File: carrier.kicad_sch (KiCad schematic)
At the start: 54 parts, among them J1 Conn_02x06_Odd_Even, J10 Conn_01x02, J11 Conn_01x02, J12 AudioJack3_SwitchTR, J13 Conn_02x06_Odd_Even, J2 Conn_01x26, J3 Conn_01x26, J4 TYPE-C-31-M-12, J5 Conn_01x02, J6 Conn_01x02, J7 Conn_01x02, J8 Conn_01x02, J9 Conn_01x02, U1 CARAVEL, U2 W25Q128JVS, U3 LP5907MFX-3.3, U4 LP5907MFX-1.8, U5 LP5907MFX-1.8, U6 LP5907MFX-3.3, U7 TPD2E001DRSR, U8 OPA340NA, U9 OPA340NA, X1 SG-5032CAN

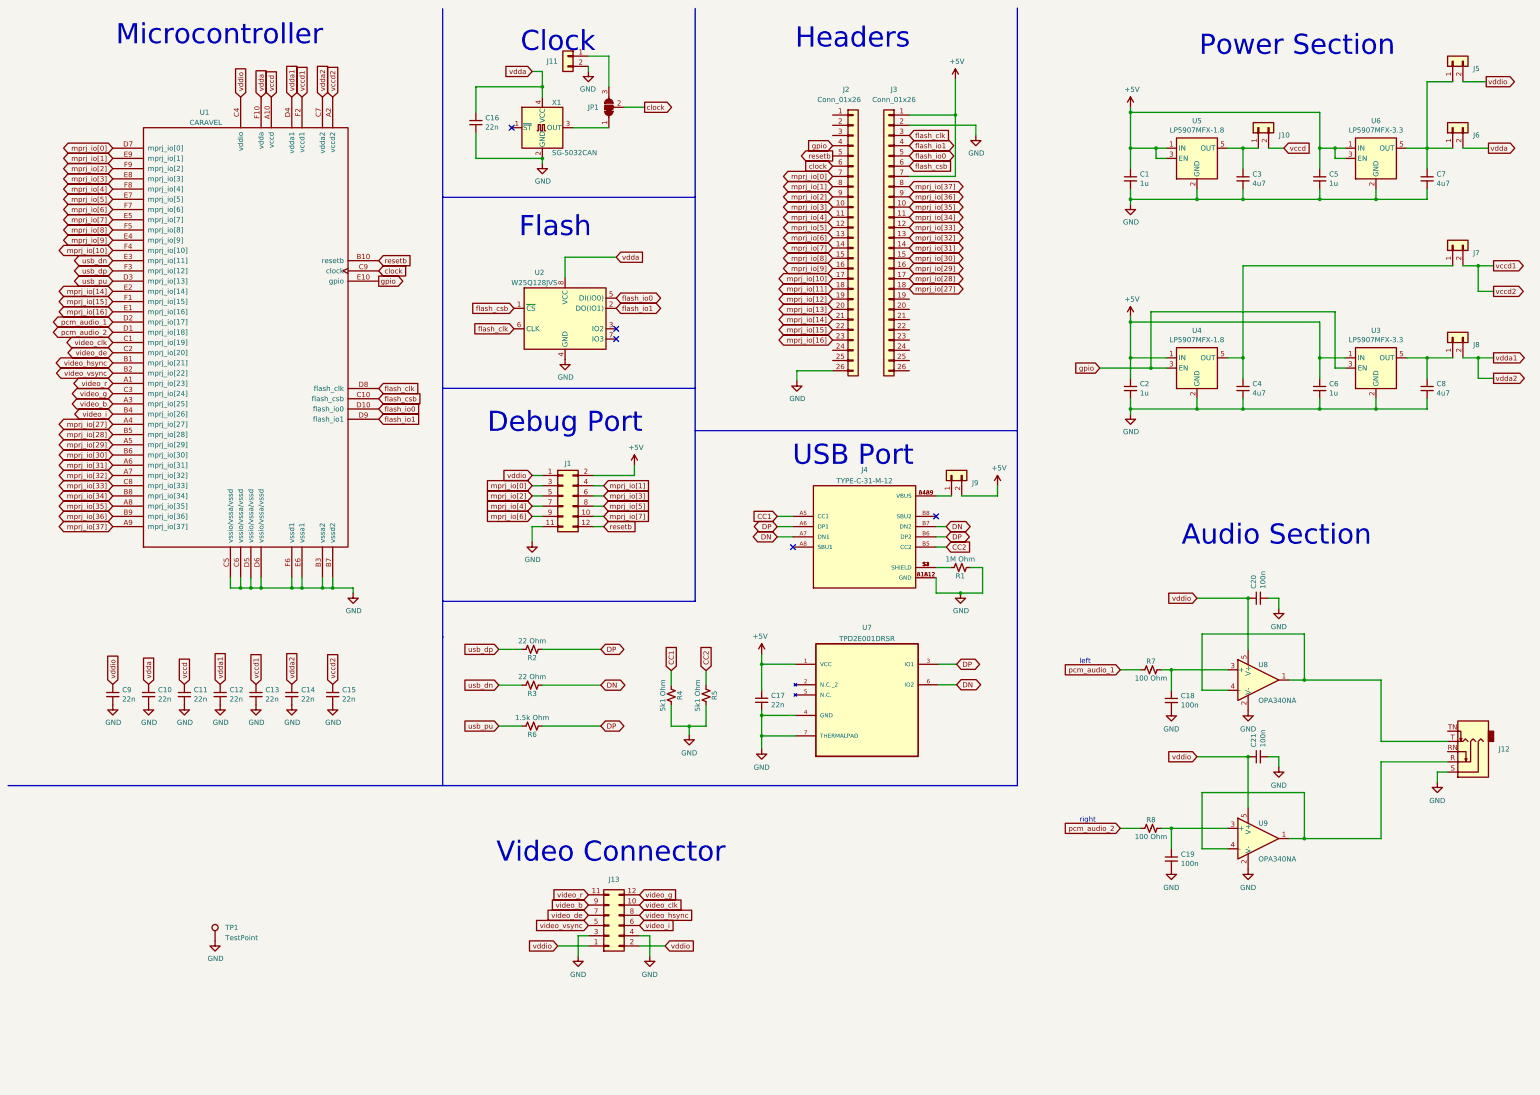
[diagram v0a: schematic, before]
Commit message: Add some buttons
May want to consider adding ESD clamps to buttons.
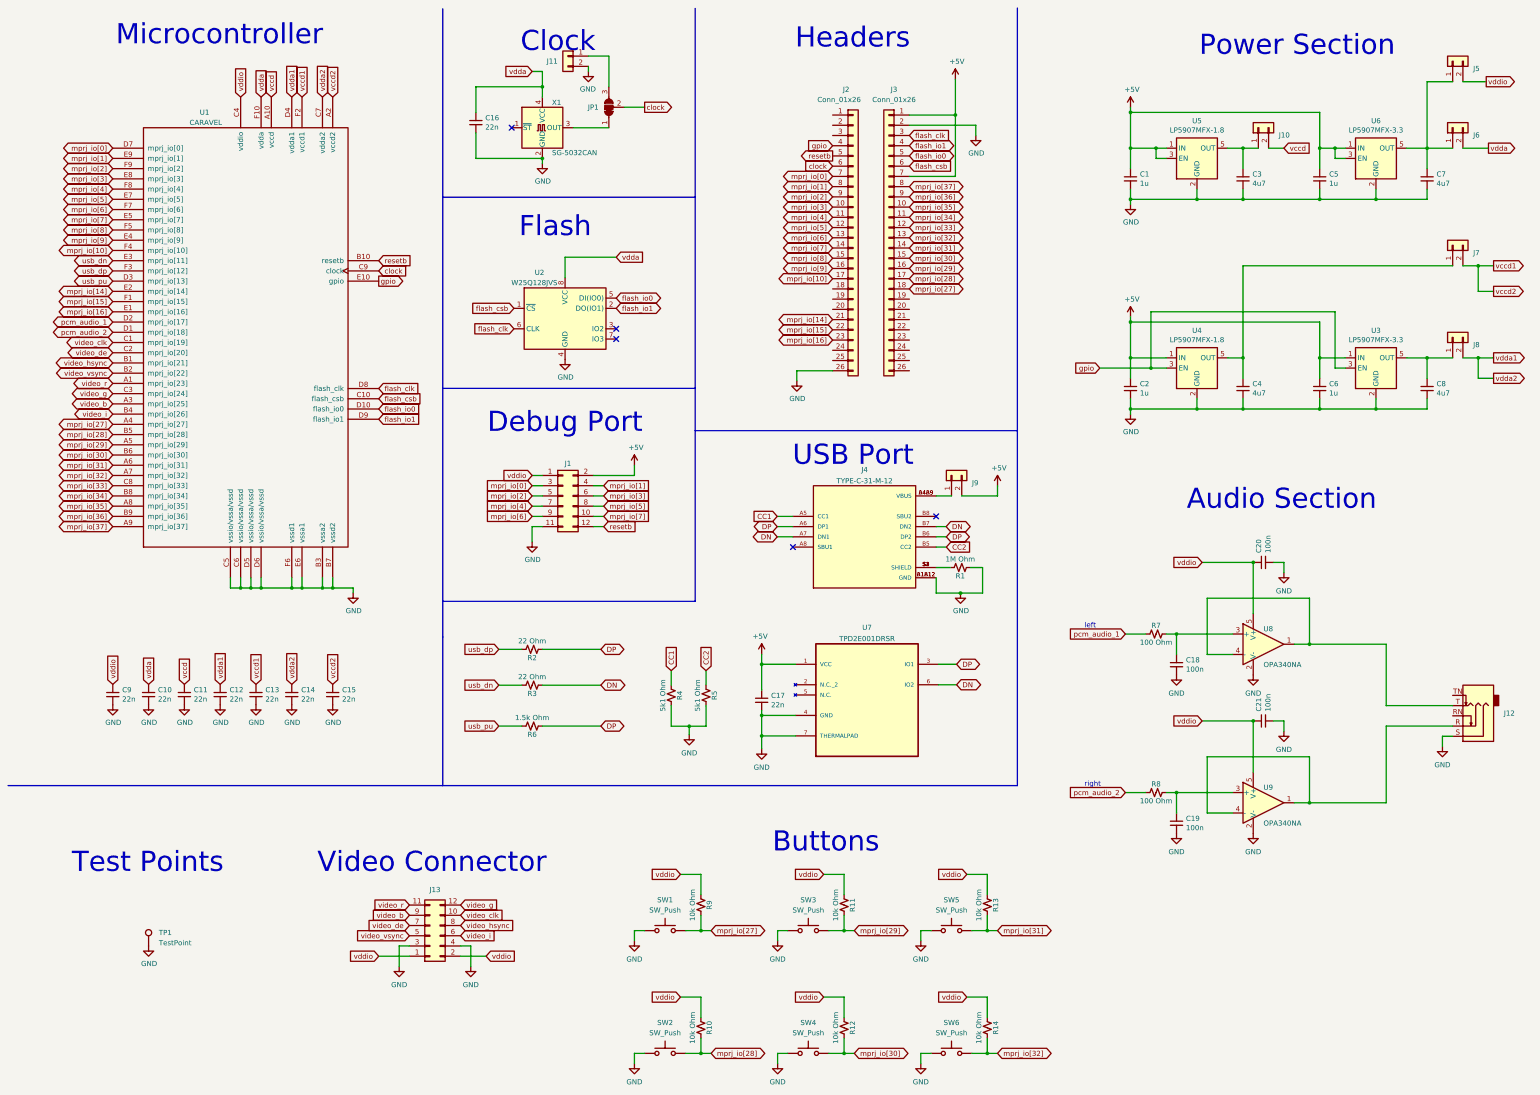
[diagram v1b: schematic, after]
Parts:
- added R10, R11, R12, R13, R14, R9: 10k Ohm, Resistor_SMD:R_0402_1005Metric, symbol Device:R_Small_US
- added SW1, SW2, SW3, SW4, SW5, SW6: SW_Push, Button_Switch_SMD:SW_Push_1P1T_NO_CK_KMR2, symbol Switch:SW_Push
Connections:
- net GND: now also SW1.1, SW2.1, SW3.1, SW4.1, SW5.1, SW6.1
- net mprj_io[27]: now also R9.1, SW1.2
- net mprj_io[28]: now also R10.1, SW2.2
- net mprj_io[29]: now also R11.1, SW3.2
- net mprj_io[30]: now also R12.1, SW4.2
- net mprj_io[31]: now also R13.1, SW5.2
- net mprj_io[32]: now also R14.1, SW6.2
- net vddio: now also R10.2, R11.2, R12.2, R13.2, R14.2, R9.2
- net mprj_io[11]: no longer names the net of J2.18 (Pin_18)
- net mprj_io[12]: no longer names the net of J2.19 (Pin_19)
- net mprj_io[13]: no longer names the net of J2.20 (Pin_20)
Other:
- note added: "Buttons"
- note added: "Test Points"
- moved on the sheet: C18, C19, C20, C21, J12, J13, R7, R8, TP1, U8, U9

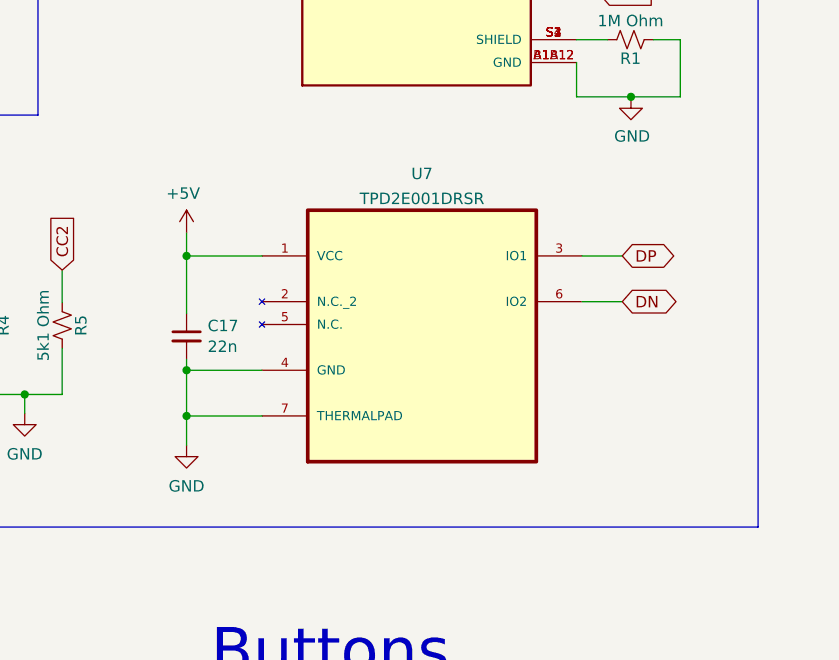
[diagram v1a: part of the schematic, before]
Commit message: schematics: Replaced TPD2E001DRSR with ESDS312DBVR
ESDS312DBVR has a better footprint which makes routing around it easier.
Also, it is much cheaper than the earlier chip used.

Fixes #13

Signed-off-by: Vedant Paranjape <22630228+VedantParanjape@users.noreply.github.com>
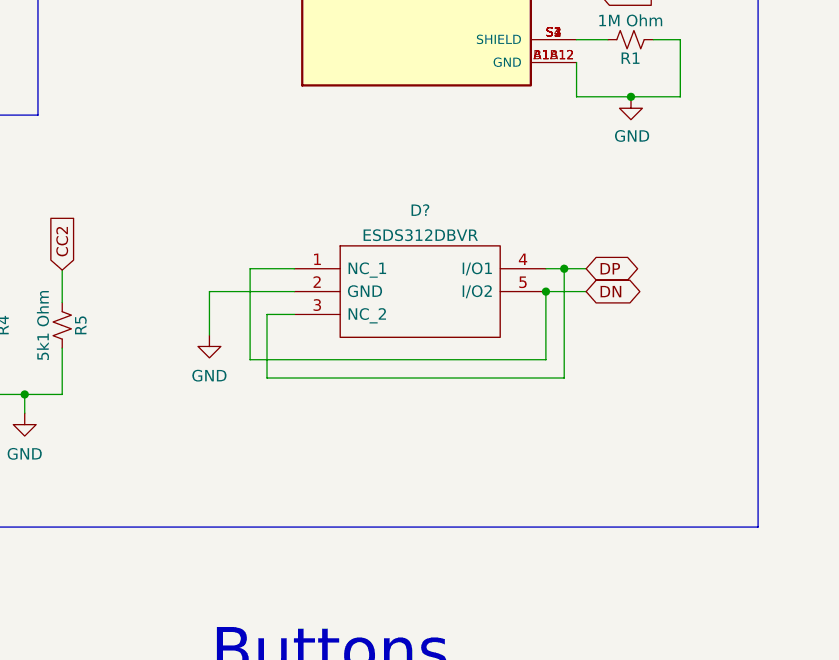
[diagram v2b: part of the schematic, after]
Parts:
- removed C17: 22n, Capacitor_SMD:C_0402_1005Metric, symbol Device:C_Small
- removed U7: TPD2E001DRSR, TPD2E001DRSR:SON95P315X315X80-7N, symbol TPD2E001DRSR:TPD2E001DRSR
- added D?: ESDS312DBVR, SOT95P280X145-5N, symbol ESDS312DBVR:ESDS312DBVR
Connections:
- net DN: now also D?.1 (NC_1), D?.5 (I/O2)
- net DP: now also D?.3 (NC_2), D?.4 (I/O1)
- net GND: now also D?.2 (GND)
